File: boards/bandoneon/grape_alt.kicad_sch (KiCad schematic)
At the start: 11 parts, among them J2 JST XH-3A, J3 JST XH-3A, U2 MCP3008

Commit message: Ready for routing
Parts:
- renumbered H4 to H20, H3 to H44, H7 to H45, H5 to H64, H2 to H65, H1 to H66, H6 to H67, J3 to J5, U2 to U8
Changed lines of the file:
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@@
   (symbol (lib_id "Library:SS39ET") (at 39.37 80.01 0) (unit 1)
     (in_bom yes) (on_board yes) (dnp no)
-    (property "Reference" "H4" (at 39.37 73.66 0)
+    (property "Reference" "H20" (at 39.37 73.66 0)
       (effects (font (size 1.27 1.27)))
     )
@@
       (project "bandoneon"
         (path "/3628cda3-bad1-4014-a851-91434ca52087/6c143dcb-6d9e-4b72-8b40-56f59ec6745c"
-          (reference "H4") (unit 1)
+          (reference "H20") (unit 1)
         )
       )
@@
   (symbol (lib_id "Library:SS39ET") (at 39.37 54.61 0) (unit 1)
     (in_bom yes) (on_board yes) (dnp no)
-    (property "Reference" "H2" (at 39.37 48.26 0)
+    (property "Reference" "H65" (at 39.37 48.26 0)
       (effects (font (size 1.27 1.27)))
     )
@@
       (project "bandoneon"
         (path "/3628cda3-bad1-4014-a851-91434ca52087/6c143dcb-6d9e-4b72-8b40-56f59ec6745c"
-          (reference "H2") (unit 1)
+          (reference "H65") (unit 1)
         )
       )
@@
   (symbol (lib_id "Library:SS39ET") (at 39.37 118.11 0) (unit 1)
     (in_bom yes) (on_board yes) (dnp no)
-    (property "Reference" "H7" (at 39.37 111.76 0)
+    (property "Reference" "H45" (at 39.37 111.76 0)
       (effects (font (size 1.27 1.27)))
     )
@@
       (project "bandoneon"
         (path "/3628cda3-bad1-4014-a851-91434ca52087/6c143dcb-6d9e-4b72-8b40-56f59ec6745c"
-          (reference "H7") (unit 1)
+          (reference "H45") (unit 1)
         )
       )
@@
   (symbol (lib_id "Library:SS39ET") (at 39.37 41.91 0) (unit 1)
     (in_bom yes) (on_board yes) (dnp no)
-    (property "Reference" "H1" (at 39.37 35.56 0)
+    (property "Reference" "H66" (at 39.37 35.56 0)
       (effects (font (size 1.27 1.27)))
     )
@@
       (project "bandoneon"
         (path "/3628cda3-bad1-4014-a851-91434ca52087/6c143dcb-6d9e-4b72-8b40-56f59ec6745c"
-          (reference "H1") (unit 1)
+          (reference "H66") (unit 1)
         )
       )
@@
   (symbol (lib_id "Library:SS39ET") (at 39.37 67.31 0) (unit 1)
     (in_bom yes) (on_board yes) (dnp no)
-    (property "Reference" "H3" (at 39.37 60.96 0)
+    (property "Reference" "H44" (at 39.37 60.96 0)
       (effects (font (size 1.27 1.27)))
     )
@@
       (project "bandoneon"
         (path "/3628cda3-bad1-4014-a851-91434ca52087/6c143dcb-6d9e-4b72-8b40-56f59ec6745c"
-          (reference "H3") (unit 1)
+          (reference "H44") (unit 1)
         )
       )
@@
   (symbol (lib_id "Analog_ADC:MCP3008") (at 87.63 67.31 0) (unit 1)
     (in_bom yes) (on_board yes) (dnp no) (fields_autoplaced)
-    (property "Reference" "U2" (at 94.9041 52.07 0)
+    (property "Reference" "U8" (at 94.9041 52.07 0)
       (effects (font (size 1.27 1.27)) (justify left))
     )
@@
       (project "bandoneon"
         (path "/3628cda3-bad1-4014-a851-91434ca52087/6c143dcb-6d9e-4b72-8b40-56f59ec6745c"
-          (reference "U2") (unit 1)
+          (reference "U8") (unit 1)
         )
       )
@@
   (symbol (lib_id "Library:SS39ET") (at 39.37 92.71 0) (unit 1)
     (in_bom yes) (on_board yes) (dnp no)
-    (property "Reference" "H5" (at 39.37 86.36 0)
+    (property "Reference" "H64" (at 39.37 86.36 0)
       (effects (font (size 1.27 1.27)))
     )
@@
       (project "bandoneon"
         (path "/3628cda3-bad1-4014-a851-91434ca52087/6c143dcb-6d9e-4b72-8b40-56f59ec6745c"
-          (reference "H5") (unit 1)
+          (reference "H64") (unit 1)
         )
       )
@@
   (symbol (lib_id "Library:SS39ET") (at 39.37 105.41 0) (unit 1)
     (in_bom yes) (on_board yes) (dnp no)
-    (property "Reference" "H6" (at 39.37 99.06 0)
+    (property "Reference" "H67" (at 39.37 99.06 0)
       (effects (font (size 1.27 1.27)))
     )
@@
       (project "bandoneon"
         (path "/3628cda3-bad1-4014-a851-91434ca52087/6c143dcb-6d9e-4b72-8b40-56f59ec6745c"
-          (reference "H6") (unit 1)
+          (reference "H67") (unit 1)
         )
       )
@@
   (symbol (lib_id "Connector:Conn_01x03_Socket") (at 53.34 29.21 180) (unit 1)
     (in_bom yes) (on_board yes) (dnp no)
-    (property "Reference" "J3" (at 54.61 20.32 0)
+    (property "Reference" "J5" (at 54.61 20.32 0)
       (effects (font (size 1.27 1.27)))
     )
@@
       (project "bandoneon"
         (path "/3628cda3-bad1-4014-a851-91434ca52087/6c143dcb-6d9e-4b72-8b40-56f59ec6745c"
-          (reference "J3") (unit 1)
-        )
-      )
+          (reference "J5") (unit 1)
+        )
+      )

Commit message: Manual routing
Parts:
- removed J2: JST XH-3A, symbol Connector:Conn_01x03_Socket
- removed J5: JST XH-3A, Connector_JST:JST_XH_B3B-XH-A_1x03_P2.50mm_Vertical, symbol Connector:Conn_01x03_Socket
- removed RV1: R_Potentiometer, symbol Device:R_Potentiometer
- renumbered H66 to H1, H65 to H2, H44 to H3, H20 to H4, H64 to H5, H67 to H6, H45 to H7, U8 to U2
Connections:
- no-connect marks 0 -> 1
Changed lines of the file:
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@@
   (junction (at 85.09 49.53) (diameter 0) (color 0 0 0 0)
   )
-  (wire (pts (xy 58.42 29.21) (xy 66.04 29.21))
-    (stroke (width 0) (type default))
-  )
+  (no_connect (at 72.39 59.69))
   (wire (pts (xy 60.96 80.01) (xy 60.96 69.85))
     (stroke (width 0) (type default))
@@
     (stroke (width 0) (type default))
   )
-  (wire (pts (xy 66.04 59.69) (xy 72.39 59.69))
-    (stroke (width 0) (type default))
-  )
   (wire (pts (xy 102.87 64.77) (xy 109.22 64.77))
     (stroke (width 0) (type default))
@@
     (stroke (width 0) (type default))
   )
-  (wire (pts (xy 66.04 29.21) (xy 66.04 59.69))
-    (stroke (width 0) (type default))
-  )
   (wire (pts (xy 92.71 85.09) (xy 92.71 87.63))
     (stroke (width 0) (type default))
@@
     (stroke (width 0) (type default))
   )
-  (wire (pts (xy 36.83 33.02) (xy 36.83 31.75))
-    (stroke (width 0) (type default))
-  )
-  (wire (pts (xy 36.83 25.4) (xy 36.83 26.67))
-    (stroke (width 0) (type default))
-  )
-  (wire (pts (xy 30.48 33.02) (xy 36.83 33.02))
-    (stroke (width 0) (type default))
-  )
   (wire (pts (xy 44.45 105.41) (xy 67.31 105.41))
     (stroke (width 0) (type default))
@@
     (stroke (width 0) (type default))
   )
-  (wire (pts (xy 30.48 25.4) (xy 36.83 25.4))
-    (stroke (width 0) (type default))
-  )
   (wire (pts (xy 60.96 69.85) (xy 72.39 69.85))
     (stroke (width 0) (type default))
@@
     (stroke (width 0) (type default))
   )
-  (wire (pts (xy 34.29 29.21) (xy 36.83 29.21))
-    (stroke (width 0) (type default))
-  )
   (wire (pts (xy 44.45 80.01) (xy 60.96 80.01))
     (stroke (width 0) (type default))
@@
   )
   (hierarchical_label "3V3" (shape input) (at 44.45 52.07 0) (fields_autoplaced)
-    (effects (font (size 1.27 1.27)) (justify left))
-  )
-  (hierarchical_label "3V3" (shape input) (at 58.42 26.67 0) (fields_autoplaced)
     (effects (font (size 1.27 1.27)) (justify left))
   )
@@
     (effects (font (size 1.27 1.27)) (justify left))
   )
-  (hierarchical_label "GND" (shape input) (at 58.42 31.75 0) (fields_autoplaced)
-    (effects (font (size 1.27 1.27)) (justify left))
-  )
   (hierarchical_label "CS" (shape input) (at 109.22 72.39 0) (fields_autoplaced)
     (effects (font (size 1.27 1.27)) (justify left))
@@
   (symbol (lib_id "Library:SS39ET") (at 39.37 80.01 0) (unit 1)
     (in_bom yes) (on_board yes) (dnp no)
-    (property "Reference" "H20" (at 39.37 73.66 0)
+    (property "Reference" "H4" (at 39.37 73.66 0)
       (effects (font (size 1.27 1.27)))
     )
@@
       (project "bandoneon"
         (path "/3628cda3-bad1-4014-a851-91434ca52087/6c143dcb-6d9e-4b72-8b40-56f59ec6745c"
-          (reference "H20") (unit 1)
+          (reference "H4") (unit 1)
         )
       )
@@
   (symbol (lib_id "Library:SS39ET") (at 39.37 54.61 0) (unit 1)
     (in_bom yes) (on_board yes) (dnp no)
-    (property "Reference" "H65" (at 39.37 48.26 0)
+    (property "Reference" "H2" (at 39.37 48.26 0)
       (effects (font (size 1.27 1.27)))
     )
@@
       (project "bandoneon"
         (path "/3628cda3-bad1-4014-a851-91434ca52087/6c143dcb-6d9e-4b72-8b40-56f59ec6745c"
-          (reference "H65") (unit 1)
+          (reference "H2") (unit 1)
         )
       )
@@
   (symbol (lib_id "Library:SS39ET") (at 39.37 118.11 0) (unit 1)
     (in_bom yes) (on_board yes) (dnp no)
-    (property "Reference" "H45" (at 39.37 111.76 0)
+    (property "Reference" "H7" (at 39.37 111.76 0)
       (effects (font (size 1.27 1.27)))
     )
@@
       (project "bandoneon"
         (path "/3628cda3-bad1-4014-a851-91434ca52087/6c143dcb-6d9e-4b72-8b40-56f59ec6745c"
-          (reference "H45") (unit 1)
-        )
-      )
-    )
-  )
-  (symbol (lib_id "Device:R_Potentiometer") (at 30.48 29.21 0) (unit 1)
-    (in_bom yes) (on_board no) (dnp no) (fields_autoplaced)
-    (property "Reference" "RV1" (at 27.94 27.94 0)
-      (effects (font (size 1.27 1.27)) (justify right))
-    )
-    (property "Value" "R_Potentiometer" (at 27.94 30.48 0)
-      (effects (font (size 1.27 1.27)) (justify right))
-    )
-    (property "Footprint" "" (at 30.48 29.21 0)
-      (effects (font (size 1.27 1.27)) hide)
-    )
-    (property "Datasheet" "~" (at 30.48 29.21 0)
-      (effects (font (size 1.27 1.27)) hide)
-    )
-    (pin "1")
-    (pin "2")
-    (pin "3")
-    (instances
-      (project "bandoneon"
-        (path "/3628cda3-bad1-4014-a851-91434ca52087/6c143dcb-6d9e-4b72-8b40-56f59ec6745c"
-          (reference "RV1") (unit 1)
-        )
-      )
-    )
-  )
-  (symbol (lib_id "Connector:Conn_01x03_Socket") (at 41.91 29.21 0) (mirror x) (unit 1)
-    (in_bom yes) (on_board no) (dnp no)
-    (property "Reference" "J2" (at 40.64 20.32 0)
-      (effects (font (size 1.27 1.27)))
-    )
-    (property "Value" "JST XH-3A" (at 41.91 22.86 0)
-      (effects (font (size 1.27 1.27)))
-    )
-    (property "Footprint" "" (at 41.91 29.21 0)
-      (effects (font (size 1.27 1.27)) hide)
-    )
-    (property "Datasheet" "~" (at 41.91 29.21 0)
-      (effects (font (size 1.27 1.27)) hide)
-    )
-    (pin "3")
-    (pin "2")
-    (pin "1")
-    (instances
-      (project "bandoneon"
-        (path "/3628cda3-bad1-4014-a851-91434ca52087/6c143dcb-6d9e-4b72-8b40-56f59ec6745c"
-          (reference "J2") (unit 1)
+          (reference "H7") (unit 1)
         )
       )
@@
   (symbol (lib_id "Library:SS39ET") (at 39.37 41.91 0) (unit 1)
     (in_bom yes) (on_board yes) (dnp no)
-    (property "Reference" "H66" (at 39.37 35.56 0)
-      (effects (font (size 1.27 1.27)))
+    (property "Reference" "H1" (at 39.37 35.56 0)
+      (effects (font (size 1.27 1.27)) hide)
     )
     (property "Value" "~" (at 40.64 40.64 0)
@@
       (project "bandoneon"
         (path "/3628cda3-bad1-4014-a851-91434ca52087/6c143dcb-6d9e-4b72-8b40-56f59ec6745c"
-          (reference "H66") (unit 1)
+          (reference "H1") (unit 1)
         )
       )
@@
   (symbol (lib_id "Library:SS39ET") (at 39.37 67.31 0) (unit 1)
     (in_bom yes) (on_board yes) (dnp no)
-    (property "Reference" "H44" (at 39.37 60.96 0)
+    (property "Reference" "H3" (at 39.37 60.96 0)
       (effects (font (size 1.27 1.27)))
     )
@@
       (project "bandoneon"
         (path "/3628cda3-bad1-4014-a851-91434ca52087/6c143dcb-6d9e-4b72-8b40-56f59ec6745c"
-          (reference "H44") (unit 1)
+          (reference "H3") (unit 1)
         )
       )
@@
   (symbol (lib_id "Analog_ADC:MCP3008") (at 87.63 67.31 0) (unit 1)
     (in_bom yes) (on_board yes) (dnp no) (fields_autoplaced)
-    (property "Reference" "U8" (at 94.9041 52.07 0)
+    (property "Reference" "U2" (at 94.9041 52.07 0)
       (effects (font (size 1.27 1.27)) (justify left))
     )
@@
       (project "bandoneon"
         (path "/3628cda3-bad1-4014-a851-91434ca52087/6c143dcb-6d9e-4b72-8b40-56f59ec6745c"
-          (reference "U8") (unit 1)
+          (reference "U2") (unit 1)
         )
       )
@@
   (symbol (lib_id "Library:SS39ET") (at 39.37 92.71 0) (unit 1)
     (in_bom yes) (on_board yes) (dnp no)
-    (property "Reference" "H64" (at 39.37 86.36 0)
+    (property "Reference" "H5" (at 39.37 86.36 0)
       (effects (font (size 1.27 1.27)))
     )
@@
       (project "bandoneon"
         (path "/3628cda3-bad1-4014-a851-91434ca52087/6c143dcb-6d9e-4b72-8b40-56f59ec6745c"
-          (reference "H64") (unit 1)
+          (reference "H5") (unit 1)
         )
       )
@@
   (symbol (lib_id "Library:SS39ET") (at 39.37 105.41 0) (unit 1)
     (in_bom yes) (on_board yes) (dnp no)
-    (property "Reference" "H67" (at 39.37 99.06 0)
+    (property "Reference" "H6" (at 39.37 99.06 0)
       (effects (font (size 1.27 1.27)))
     )
@@
       (project "bandoneon"
         (path "/3628cda3-bad1-4014-a851-91434ca52087/6c143dcb-6d9e-4b72-8b40-56f59ec6745c"
-          (reference "H67") (unit 1)
-        )
-      )
-    )
-  )
-  (symbol (lib_id "Connector:Conn_01x03_Socket") (at 53.34 29.21 180) (unit 1)
-    (in_bom yes) (on_board yes) (dnp no)
-    (property "Reference" "J5" (at 54.61 20.32 0)
-      (effects (font (size 1.27 1.27)))
-    )
-    (property "Value" "JST XH-3A" (at 53.34 22.86 0)
-      (effects (font (size 1.27 1.27)))
-    )
-    (property "Footprint" "Connector_JST:JST_XH_B3B-XH-A_1x03_P2.50mm_Vertical" (at 53.34 29.21 0)
-      (effects (font (size 1.27 1.27)) hide)
-    )
-    (property "Datasheet" "~" (at 53.34 29.21 0)
-      (effects (font (size 1.27 1.27)) hide)
-    )
-    (pin "3")
-    (pin "2")
-    (pin "1")
-    (instances
-      (project "bandoneon"
-        (path "/3628cda3-bad1-4014-a851-91434ca52087/6c143dcb-6d9e-4b72-8b40-56f59ec6745c"
-          (reference "J5") (unit 1)
-        )
-      )
+          (reference "H6") (unit 1)
+        )
+      )

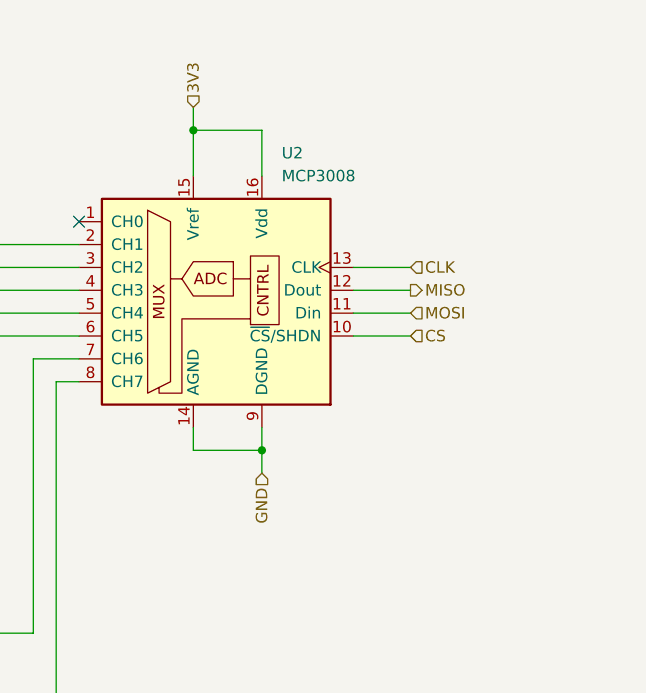
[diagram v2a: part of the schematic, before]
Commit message: Add models and ground plane
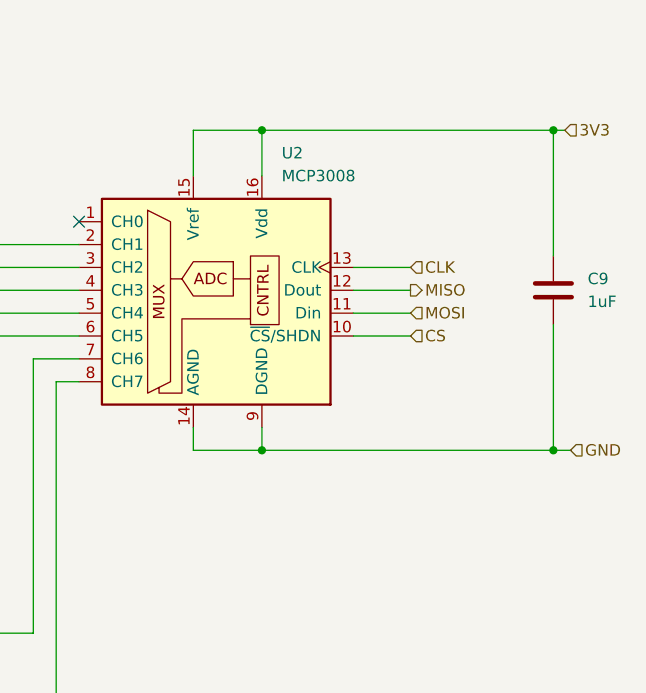
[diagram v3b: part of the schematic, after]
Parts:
- added C9: 1uF, symbol Device:C
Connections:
- net 3V3: now also C9.1
- net GND: now also C9.2
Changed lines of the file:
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@@
 (kicad_sch (version 20230121) (generator eeschema)
   (paper "A5")
+  (junction (at 125.095 49.53) (diameter 0) (color 0 0 0 0)
+  )
   (junction (at 92.71 85.09) (diameter 0) (color 0 0 0 0)
   )
-  (junction (at 85.09 49.53) (diameter 0) (color 0 0 0 0)
+  (junction (at 92.71 49.53) (diameter 0) (color 0 0 0 0)
+  )
+  (junction (at 125.095 85.09) (diameter 0) (color 0 0 0 0)
   )
   (no_connect (at 72.39 59.69))
@@
     (stroke (width 0) (type default))
   )
+  (wire (pts (xy 125.095 71.12) (xy 125.095 85.09))
+    (stroke (width 0) (type default))
+  )
   (wire (pts (xy 102.87 64.77) (xy 109.22 64.77))
     (stroke (width 0) (type default))
@@
     (stroke (width 0) (type default))
   )
+  (wire (pts (xy 125.095 85.09) (xy 127 85.09))
+    (stroke (width 0) (type default))
+  )
+  (wire (pts (xy 126.365 49.53) (xy 125.095 49.53))
+    (stroke (width 0) (type default))
+  )
   (wire (pts (xy 63.5 41.91) (xy 63.5 62.23))
     (stroke (width 0) (type default))
@@
     (stroke (width 0) (type default))
   )
-  (wire (pts (xy 92.71 85.09) (xy 92.71 87.63))
-    (stroke (width 0) (type default))
-  )
   (wire (pts (xy 92.71 54.61) (xy 92.71 49.53))
     (stroke (width 0) (type default))
   )
-  (wire (pts (xy 85.09 46.99) (xy 85.09 49.53))
-    (stroke (width 0) (type default))
-  )
   (wire (pts (xy 44.45 105.41) (xy 67.31 105.41))
     (stroke (width 0) (type default))
@@
     (stroke (width 0) (type default))
   )
+  (wire (pts (xy 92.71 85.09) (xy 125.095 85.09))
+    (stroke (width 0) (type default))
+  )
   (wire (pts (xy 69.85 118.11) (xy 69.85 77.47))
     (stroke (width 0) (type default))
@@
     (stroke (width 0) (type default))
   )
+  (wire (pts (xy 125.095 49.53) (xy 125.095 63.5))
+    (stroke (width 0) (type default))
+  )
   (wire (pts (xy 85.09 82.55) (xy 85.09 85.09))
     (stroke (width 0) (type default))
@@
     (stroke (width 0) (type default))
   )
+  (wire (pts (xy 92.71 49.53) (xy 125.095 49.53))
+    (stroke (width 0) (type default))
+  )
   (wire (pts (xy 44.45 80.01) (xy 60.96 80.01))
     (stroke (width 0) (type default))
@@
     (effects (font (size 1.27 1.27)) (justify left))
   )
-  (hierarchical_label "GND" (shape input) (at 92.71 87.63 270) (fields_autoplaced)
-    (effects (font (size 1.27 1.27)) (justify right))
+  (hierarchical_label "3V3" (shape input) (at 126.365 49.53 0) (fields_autoplaced)
+    (effects (font (size 1.27 1.27)) (justify left))
   )
   (hierarchical_label "MOSI" (shape input) (at 109.22 69.85 0) (fields_autoplaced)
     (effects (font (size 1.27 1.27)) (justify left))
   )
+  (hierarchical_label "GND" (shape input) (at 127 85.09 0) (fields_autoplaced)
+    (effects (font (size 1.27 1.27)) (justify left))
+  )
   (hierarchical_label "CLK" (shape input) (at 109.22 64.77 0) (fields_autoplaced)
     (effects (font (size 1.27 1.27)) (justify left))
@@
   )
   (hierarchical_label "GND" (shape input) (at 44.45 44.45 0) (fields_autoplaced)
-    (effects (font (size 1.27 1.27)) (justify left))
-  )
-  (hierarchical_label "3V3" (shape input) (at 85.09 46.99 90) (fields_autoplaced)
     (effects (font (size 1.27 1.27)) (justify left))
   )
@@
         )
       )
+    )
+  )
+  (symbol (lib_id "Device:C") (at 125.095 67.31 0) (unit 1)
+    (in_bom yes) (on_board yes) (dnp no) (fields_autoplaced)
+    (property "Reference" "C9" (at 128.905 66.04 0)
+      (effects (font (size 1.27 1.27)) (justify left))
+    )
+    (property "Value" "1uF" (at 128.905 68.58 0)
+      (effects (font (size 1.27 1.27)) (justify left))
+    )
+    (property "Footprint" "" (at 126.0602 71.12 0)
+      (effects (font (size 1.27 1.27)) hide)
+    )
+    (property "Datasheet" "~" (at 125.095 67.31 0)
+      (effects (font (size 1.27 1.27)) hide)
+    )
+    (pin "2")
+    (pin "1")
+    (instances
+      (project "bandoneon"
+        (path "/3628cda3-bad1-4014-a851-91434ca52087/6c143dcb-6d9e-4b72-8b40-56f59ec6745c"
+          (reference "C9") (unit 1)
+        )
+      )

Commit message: Complete manual wire
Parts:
- C9: footprint (none) -> Capacitor_SMD:C_0402_1005Metric
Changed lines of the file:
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@@
       (effects (font (size 1.27 1.27)) (justify left))
     )
-    (property "Footprint" "" (at 126.0602 71.12 0)
+    (property "Footprint" "Capacitor_SMD:C_0402_1005Metric" (at 126.0602 71.12 0)
       (effects (font (size 1.27 1.27)) hide)
     )

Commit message: Add esd protection
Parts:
- U2: LCSC (none) -> C1520159; Vendor Page (none) -> https://jlcpcb.com/partdetail/MicrochipTech-MCP3008_ISL/C15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
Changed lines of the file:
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@@
+      (effects (font (size 1.27 1.27)) hide)
+    )
+    (property "LCSC" "C1520159" (at 87.63 67.31 0)
+      (effects (font (size 1.27 1.27)) hide)
+    )
+    (property "Vendor Page" "https://jlcpcb.com/partdetail/MicrochipTech-MCP3008_ISL/C1520159" (at 87.63 67.31 0)
       (effects (font (size 1.27 1.27)) hide)
     )
